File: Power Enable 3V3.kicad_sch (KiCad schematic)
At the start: 20 parts, among them Q19 DMN2004K, U3 MAX17502EATB+T, U4 TLV75733PDBV, U5 LM66100DCKR, U6 LM66100DCKR

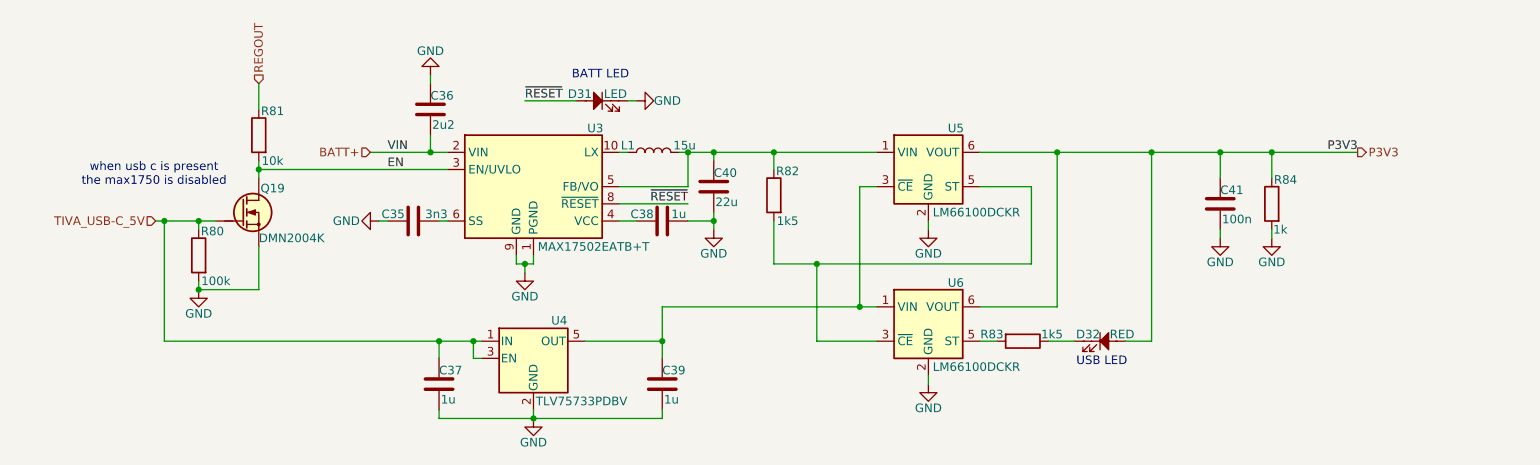
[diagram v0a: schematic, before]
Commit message: commit before simplifying and removing features
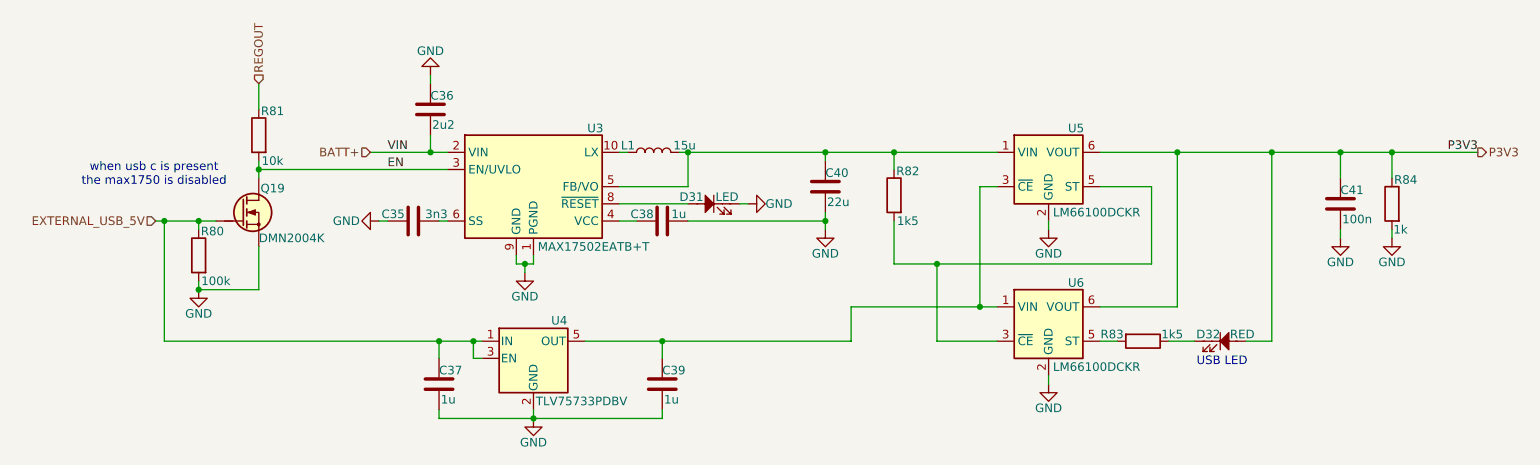
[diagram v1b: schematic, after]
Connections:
- net TIVA_USB-C_5V renamed EXTERNAL_USB_5V
- net ~{RESET}: no longer names the net of D31.2, U3.8 (~{RESET})
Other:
- note removed: "BATT LED"
- moved on the sheet: C40, C41, D31, D32, R82, R83, R84, U5, U6
